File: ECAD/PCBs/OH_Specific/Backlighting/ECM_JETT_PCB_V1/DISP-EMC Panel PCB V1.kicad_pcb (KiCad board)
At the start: 2 copper layers, 110.3 x 171.8 mm, 149 parts, among them J1 Conn_01x04_Female, J2 Conn_01x04_Female, J3 Conn_01x02_Female, SW1 PT_Tactile_Switch_Led

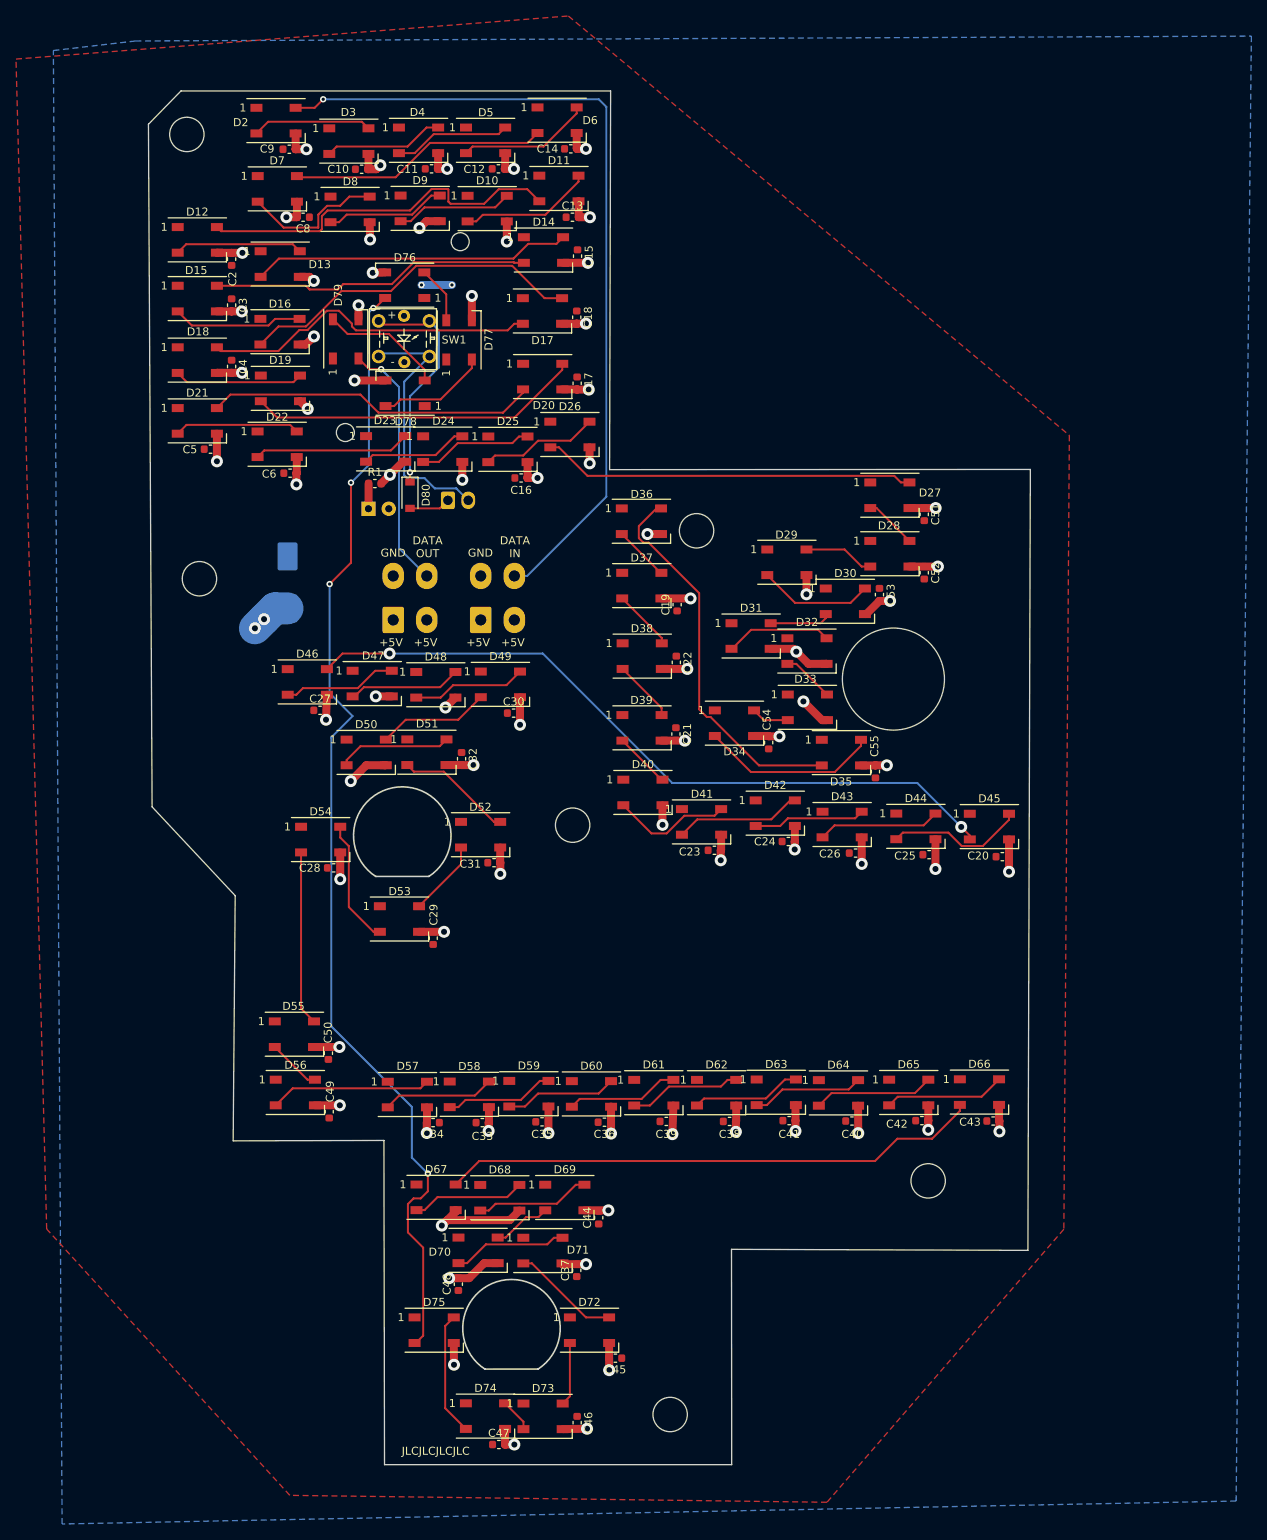
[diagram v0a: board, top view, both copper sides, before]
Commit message: LIP Nears Release Candidate
Center Pedestal Complete...need to add limit switches for rudder linear actuator, and create assembly that assembles the UIP and LIP together prior to top level assembly.

Working against #350
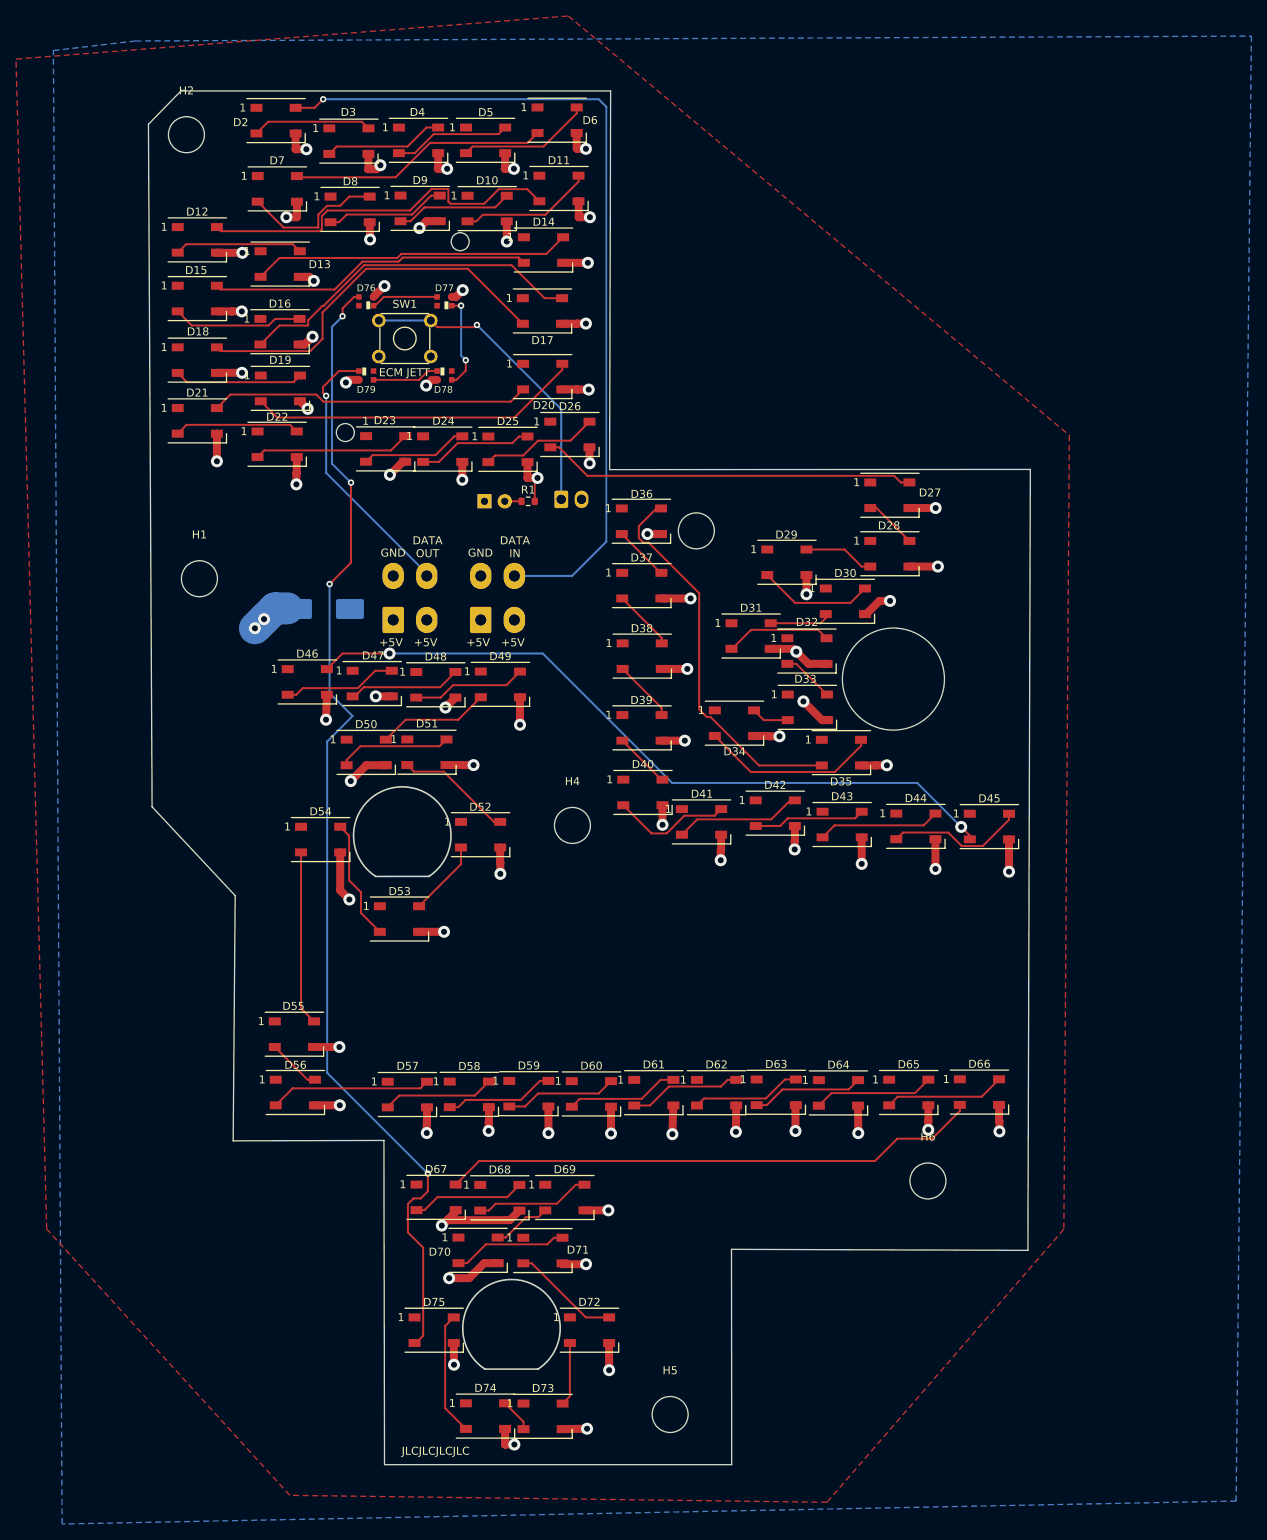
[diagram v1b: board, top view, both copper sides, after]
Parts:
- removed 1, 3 (x2), 4, 5, 6: OH_Panel_Fastner_Keepout, OH_Backlighting:OH_Panel_6-32_PHS
- removed C10, C11, C12, C13, C14, C15, C16, C17, C18, C19, C2, C20, C21, C22, C23, C24, C25, C26, C27, C28, C29, C3, C30, C31, C32, C33, C34, C35, C36, C37, C38, C39, C4, C40, C41, C42, C43, C44, C45, C46, C47, C48, C49, C5, C50, C51, C52, C53, C54, C55, C6, C8, C9: C, Capacitor_SMD:C_0603_1608Metric
- removed D80: D, Diode_SMD:D_SOD-123
- removed G***: LOGO, OH_General:OH_LOGO_37.7mm_5.9mm
- removed G***: S2AL Toggle, OH_Backlighting:S2AL_Toggle_Silkscreen
- removed G***: LOGO, OH_General:CC-BY-NC-SA-Small
- removed G1: S3AL Toggle, OH_Backlighting:S3AL_Toggle_Silkscreen
- added H1: MountingHole, MountingHole:MountingHole_4.5mm, F.Cu at (51.0, 69.7)
- added H2: MountingHole, MountingHole:MountingHole_4.5mm, F.Cu at (49.4, 14.2)
- added H3: MountingHole, MountingHole:MountingHole_4.5mm, B.Cu at (113.1, 63.8)
- added H4: MountingHole, MountingHole:MountingHole_4.5mm, F.Cu at (97.6, 100.6)
- added H5: MountingHole, MountingHole:MountingHole_4.5mm, F.Cu at (109.8, 174.2)
- added H6: MountingHole, MountingHole:MountingHole_4.5mm, F.Cu at (142.1, 145.0)
- C1: value C_Polarized -> 1000 nF
- D1: value LED -> READY
- D76, D77, D78, D79: value WS2812B -> LED; footprint LED_SMD:LED_WS2812B_PLCC4_5.0x5.0mm_P3.2mm -> KiCAD Libraries:WS2812-2020
- J1: value Conn_01x04_Female -> BL IN
- J2: value Conn_01x04_Female -> BL OUT
- J3: value Conn_01x02_Female -> ECM JETT
- SW1: value PT_Tactile_Switch_Led -> ECM JETT; footprint PT_Library_v001:PT_Small_Tactile_Switch_With_LED -> Button_Switch_THT:SW_TH_Tactile_Omron_B3F-10xx
- moved R1 19.3 mm to (92.1, 60.1)
- moved D1 14.5 mm to (86.6, 60.1)
- moved J3 14.2 mm to (96.2, 59.8)
- moved C1 5.64 mm to (66.5, 73.5), turned to 0 degrees
- moved D78 5.40 mm to (81.6, 44.3)
- moved D79 5.24 mm to (71.8, 44.3), turned to 180 degrees
- moved D76 5.22 mm to (71.8, 35.1), turned to 0 degrees
- moved D77 5.16 mm to (81.6, 35.1), turned to 0 degrees
- moved SW1 3.92 mm to (73.4, 37.5)
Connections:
- D1 pad 1: Net-(D1-Pad1) -> /LED+5V
- D1 pad 2: /LED+5V -> Net-(D1-Pad2)
- D76 pad 1: /LED+5V -> Net-(D76-Pad1)
- D76 pad 2: Net-(D76-Pad2) -> /LEDGND
- D76 pad 3: /LEDGND -> Net-(D75-Pad2)
- D76 pad 4: Net-(D75-Pad2) -> /LED+5V
- D77 pad 1: /LED+5V -> Net-(D77-Pad1)
- D77 pad 2: Net-(D77-Pad2) -> /LEDGND
- D77 pad 3: /LEDGND -> Net-(D76-Pad1)
- D77 pad 4: Net-(D76-Pad2) -> /LED+5V
- D78 pad 1: /LED+5V -> Net-(D78-Pad1)
- D78 pad 2: Net-(D78-Pad2) -> /LEDGND
- D78 pad 3: /LEDGND -> Net-(D77-Pad1)
- D78 pad 4: Net-(D77-Pad2) -> /LED+5V
- D79 pad 1: /LED+5V -> /DATAOUT
- D79 pad 2: /DATAOUT -> /LEDGND
- D79 pad 3: /LEDGND -> Net-(D78-Pad1)
- D79 pad 4: Net-(D78-Pad2) -> /LED+5V
- J3 pad 1: /Column1 -> /SW_JETT
- J3 pad 2: /Row1 -> /LEDGND
- R1 pad 1: Net-(D1-Pad1) -> Net-(D1-Pad2)
- SW1 pad 1: Net-(D80-Pad1) -> /SW_JETT
- SW1 pad 2: Net-(D80-Pad1) -> /SW_JETT
- SW1 pad 3: /Row1 -> /LEDGND
- SW1 pad 4: /Row1 -> /LEDGND
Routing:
- net /SW_JETT: track 0.00 -> 40.2 mm, vias 0 -> 1
- net /Row1: track 32.1 -> 0.00 mm
- net Net-(D80-Pad1): track 28.8 -> 0.00 mm, vias 1 -> 0
- net Net-(D78-Pad2): track 15.4 -> 0.00 mm
- net Net-(D77-Pad2): track 13.8 -> 0.00 mm
- net Net-(D77-Pad1): track 0.00 -> 11.8 mm, vias 0 -> 2
- net Net-(D76-Pad1): track 0.00 -> 8.40 mm
- net Net-(D78-Pad1): track 0.00 -> 8.40 mm
- net Net-(D76-Pad2): track 7.13 -> 0.00 mm
- net Net-(D17-Pad2): track 42.1 -> 47.5 mm
- net /Column1: track 5.16 -> 0.00 mm
- net /LED+5V: track 8.92 -> 5.11 mm, vias 4 -> 2
- net /DATAIN: track 104.0 -> 107.3 mm
- net Net-(D1-Pad1): track 3.16 -> 0.00 mm
- net /DATAOUT: track 31.6 -> 34.3 mm
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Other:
- board text added: "Version 2.5"
- board text removed: "Version 2.0"

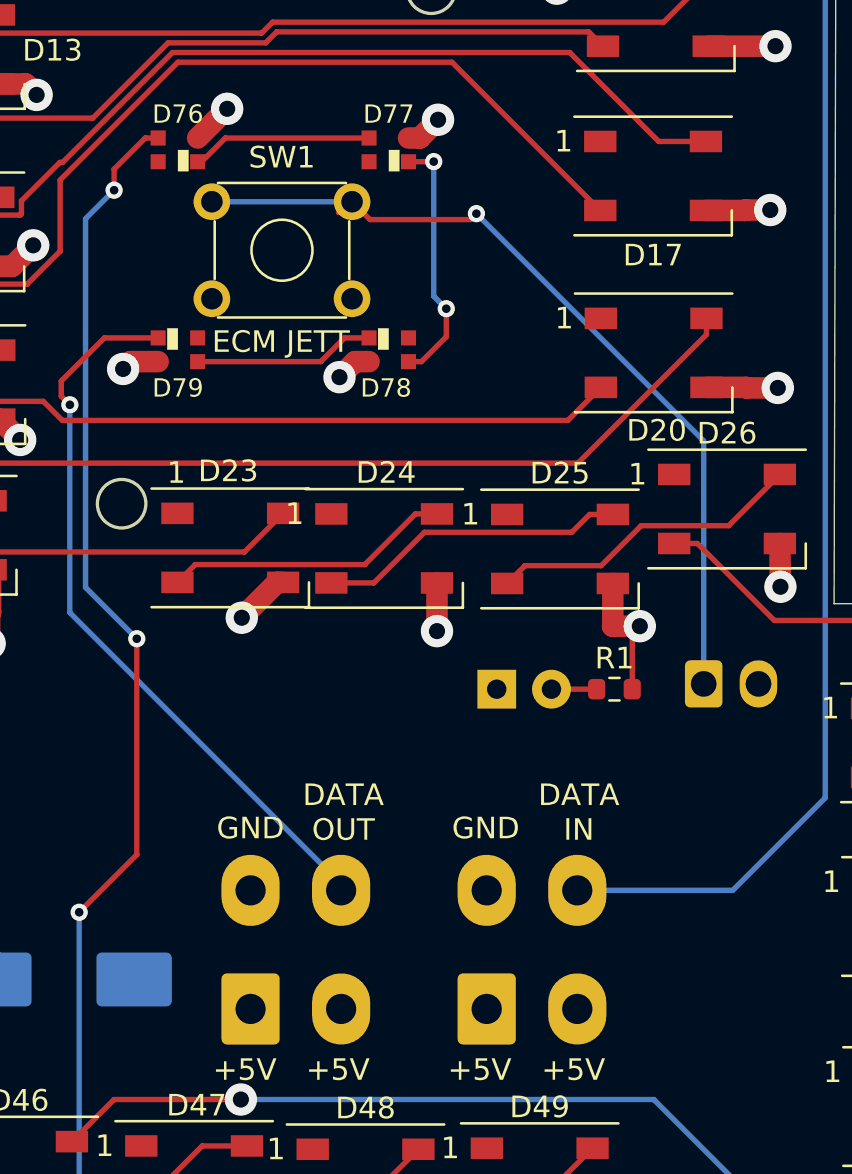
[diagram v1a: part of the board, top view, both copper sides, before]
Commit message: DISP ECM Jett Backlighting PCB Update
Changed - WS2812B-2020 LED footprint and schematic pin layout to match data sheet.
Changed - Version from 2.5 to 2.6
Changed - Manufacturing files to match.
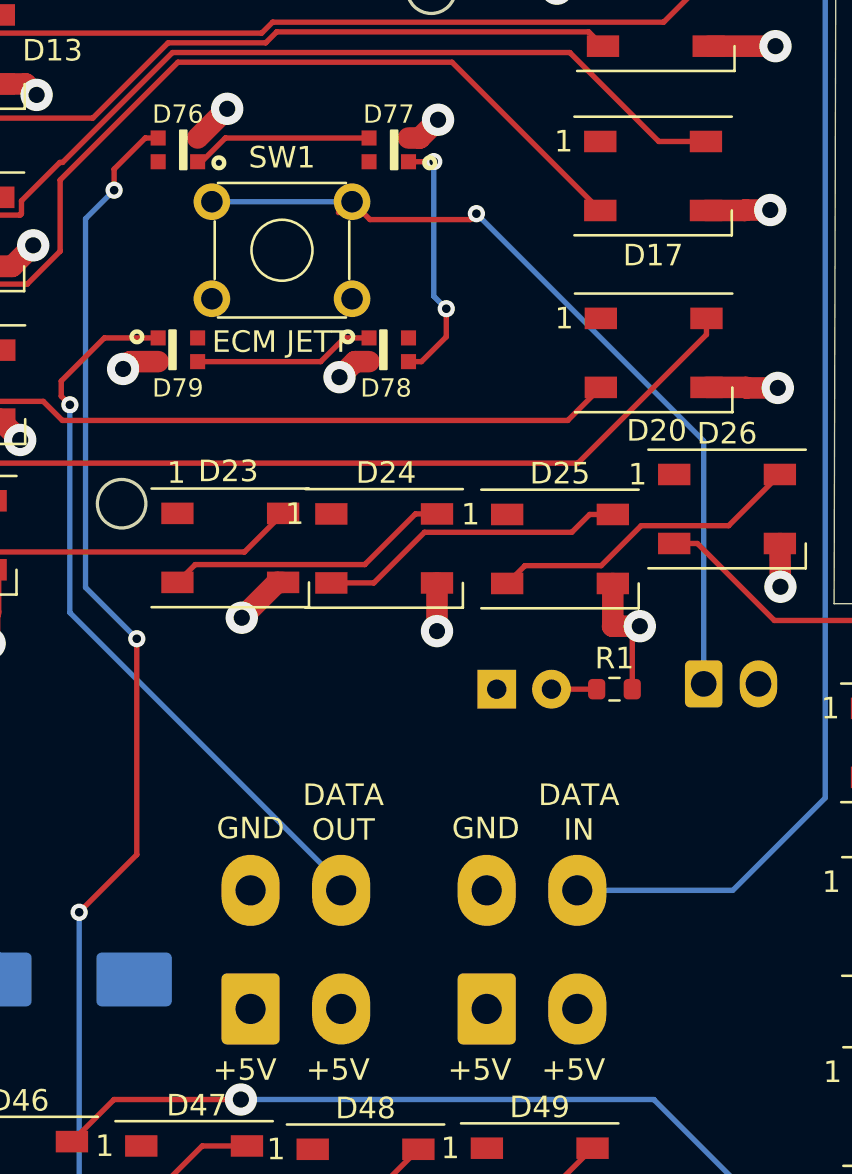
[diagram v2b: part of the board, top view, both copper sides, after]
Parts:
- D76, D77, D78, D79: footprint KiCAD Libraries:WS2812-2020 -> Openhornet:WS2812-2020
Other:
- board text added: "Version 2.6"
- board text removed: "Version 2.5"
